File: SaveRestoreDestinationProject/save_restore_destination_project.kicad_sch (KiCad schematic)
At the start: 0 parts

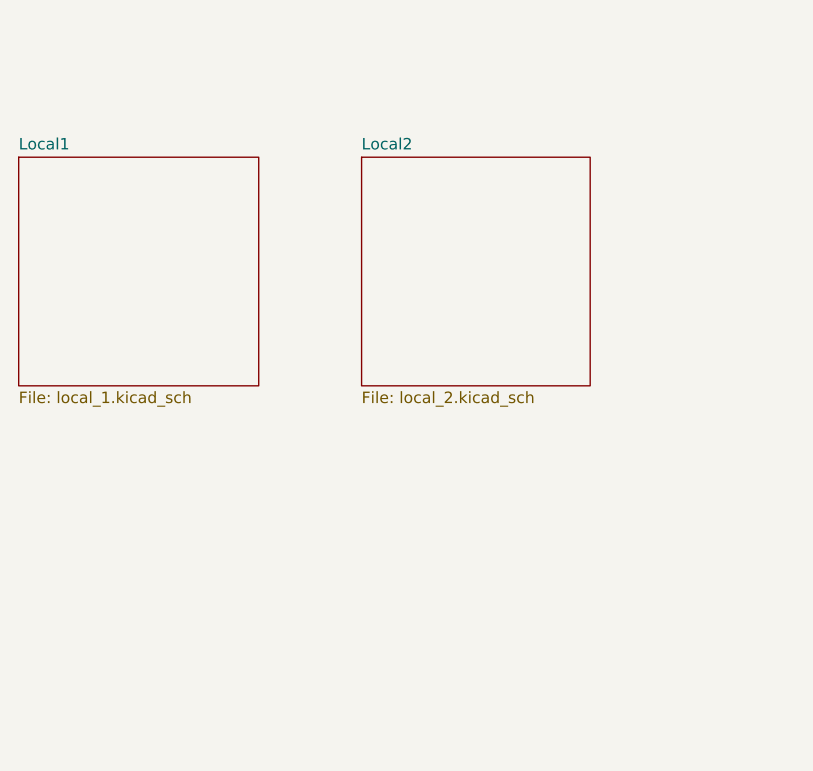
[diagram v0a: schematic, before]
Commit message: Add support for connected drawings, update test template
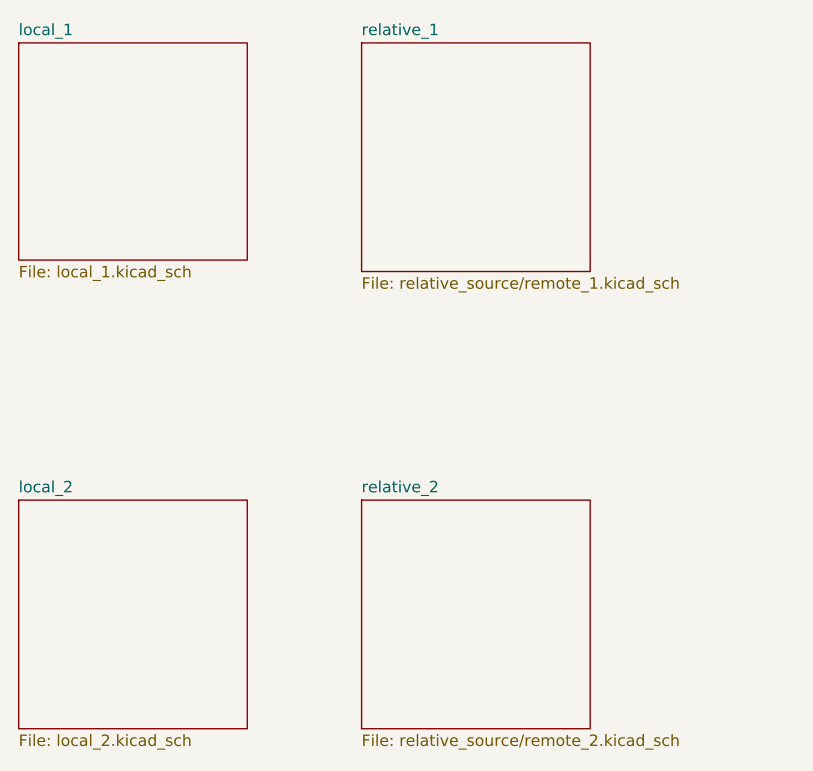
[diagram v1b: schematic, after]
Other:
- removed sheet Local1
- removed sheet Local2
- added sheet local_1 (local_1.kicad_sch)
- added sheet local_2 (local_2.kicad_sch)
- added sheet relative_1 (relative_source/remote_1.kicad_sch)
- added sheet relative_2 (relative_source/remote_2.kicad_sch)
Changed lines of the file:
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@@
-(kicad_sch (version 20230121) (generator eeschema)
-  (paper "A4")
-  (sheet (at 50.8 38.1) (size 26.67 25.4) (fields_autoplaced)
-    (stroke (width 0.1524) (type solid))
-    (fill (color 0 0 0 0.0000))
-    (property "Sheetname" "Local1" (at 50.8 37.3884 0)
-      (effects (font (size 1.27 1.27)) (justify left bottom))
-    )
-    (property "Sheetfile" "local_1.kicad_sch" (at 50.8 64.0846 0)
-      (effects (font (size 1.27 1.27)) (justify left top))
-    )
-    (instances
-      (project "save_restore_destination_project"
-        (path "/e63e39d7-6ac0-4ffd-8aa3-1841a4541b55" (page "2"))
-      )
-    )
-  )
-  (sheet (at 88.9 38.1) (size 25.4 25.4) (fields_autoplaced)
-    (stroke (width 0.1524) (type solid))
-    (fill (color 0 0 0 0.0000))
-    (property "Sheetname" "Local2" (at 88.9 37.3884 0)
-      (effects (font (size 1.27 1.27)) (justify left bottom))
-    )
-    (property "Sheetfile" "local_2.kicad_sch" (at 88.9 64.0846 0)
-      (effects (font (size 1.27 1.27)) (justify left top))
-    )
-    (instances
-      (project "save_restore_destination_project"
-        (path "/e63e39d7-6ac0-4ffd-8aa3-1841a4541b55" (page "5"))
-      )
-    )
-  )
-  (sheet_instances
-    (path "/" (page "1"))
-  )
+(kicad_sch
+	(version 20231120)
+	(generator "eeschema")
+	(generator_version "8.0")
+	(paper "A4")
+	(sheet
+		(at 88.9 25.4)
+		(size 25.4 25.4)
+		(fields_autoplaced yes)
+		(stroke
+			(width 0.1524)
+			(type solid)
+		)
+		(fill
+			(color 0 0 0 0.0000)
+		)
+		(property "Sheetname" "relative_1"
+			(at 88.9 24.6884 0)
+			(effects
+				(font
+					(size 1.27 1.27)
+				)
+				(justify left bottom)
+			)
+		)
+		(property "Sheetfile" "relative_source/remote_1.kicad_sch"
+			(at 88.9 51.3846 0)
+			(effects
+				(font
+					(size 1.27 1.27)
+				)
+				(justify left top)
+			)
+		)
+		(instances
+			(project "save_restore_destination_project"
+				(path "/7413d3c9-b6cd-43bb-b083-7571861f5f72"
+					(page "6")
+				)
+			)
+		)
+	)
+	(sheet
+		(at 50.8 25.4)
+		(size 25.4 24.13)
+		(fields_autoplaced yes)
+		(stroke
+			(width 0.1524)
+			(type solid)
+		)
+		(fill
+			(color 0 0 0 0.0000)
+		)
+		(property "Sheetname" "local_1"
+			(at 50.8 24.6884 0)
+			(effects
+				(font
+					(size 1.27 1.27)
+				)
+				(justify left bottom)
+			)
+		)
+		(property "Sheetfile" "local_1.kicad_sch"
+			(at 50.8 50.1146 0)
+			(effects
+				(font
+					(size 1.27 1.27)
+				)
+				(justify left top)
+			)
+		)
+		(instances
+			(project "save_restore_destination_project"
+				(path "/7413d3c9-b6cd-43bb-b083-7571861f5f72"
+					(page "2")
+				)
+			)
+		)
+	)
+	(sheet
+		(at 88.9 76.2)
+		(size 25.4 25.4)
+		(fields_autoplaced yes)
+		(stroke
+			(width 0.1524)
+			(type solid)
+		)
+		(fill
+			(color 0 0 0 0.0000)
+		)
+		(property "Sheetname" "relative_2"
+			(at 88.9 75.4884 0)
+			(effects
+				(font
+					(size 1.27 1.27)
+				)
+				(justify left bottom)
+			)
+		)
+		(property "Sheetfile" "relative_source/remote_2.kicad_sch"
+			(at 88.9 102.1846 0)
+			(effects
+				(font
+					(size 1.27 1.27)
+				)
+				(justify left top)
+			)
+		)
+		(instances
+			(project "save_restore_destination_project"
+				(path "/7413d3c9-b6cd-43bb-b083-7571861f5f72"
+					(page "8")
+				)
+			)
+		)
+	)
+	(sheet
+		(at 50.8 76.2)
+		(size 25.4 25.4)
+		(fields_autoplaced yes)
+		(stroke
+			(width 0.1524)
+			(type solid)
+		)
+		(fill
+			(color 0 0 0 0.0000)
+		)
+		(property "Sheetname" "local_2"
+			(at 50.8 75.4884 0)
+			(effects
+				(font
+					(size 1.27 1.27)
+				)
+				(justify left bottom)
+			)
+		)
+		(property "Sheetfile" "local_2.kicad_sch"
+			(at 50.8 102.1846 0)
+			(effects
+				(font
+					(size 1.27 1.27)
+				)
+				(justify left top)
+			)
+		)
+		(instances
+			(project "save_restore_destination_project"
+				(path "/7413d3c9-b6cd-43bb-b083-7571861f5f72"
+					(page "5")
+				)
+			)
+		)
+	)
+	(sheet_instances
+		(path "/"
+			(page "1")
+		)
+	)
 )
